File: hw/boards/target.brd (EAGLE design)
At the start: 25.4 x 25.4 mm, 21 parts, among them T1 771-BC847BS-T/R, U1 579-MCP1703T-3002ECB, U2 771-LPC824M201JDH20J, U4 579-MCP6291T-E/OT, X1 798-DF134P125V20

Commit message: Fix some part numbers
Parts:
- removed X1: 798-DF134P125V20, con-molex:53398-04
- added JP3: FTSH-105-01-L, torpedo:FTSH-105-01-XXX-DV-K
- JP2: value FTSH-105-01-L -> 798-DF134P125V20; device torpedo:FTSH-105-01-XXX-DV-K -> con-molex:53398-04
- moved JP2 12.6 mm to (21.6, 12.7)
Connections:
- net +3V3: now also JP3.1; no longer JP2.1
- net GND: now also JP2.4, JP3.3, JP3.5, JP3.9; no longer JP2.3, JP2.5, JP2.9, X1.4
- net RST: now also JP3.10; no longer JP2.10
- net RX: now also JP2.3; no longer X1.3
- net SWCLK: now also JP3.4; no longer JP2.4
- net SWDIO: now also JP3.2; no longer JP2.2
- net TX: now also JP2.2; no longer X1.2
- net VIN: now also JP2.1; no longer X1.1
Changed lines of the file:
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@@
 <attribute name="OC_FARNELL" value="1125367" x="3.81" y="12.7" size="1.778" layer="28" rot="MR270" display="off"/>
 </element>
-<element name="JP2" library="torpedo" package="FTSH-105-01-XXX-DV-K" value="FTSH-105-01-L" x="12.7" y="21.59" rot="MR90"/>
+<element name="JP3" library="torpedo" package="FTSH-105-01-XXX-DV-K" value="FTSH-105-01-L" x="12.7" y="21.59" rot="MR90"/>
 <element name="LOGO2" library="ohw-logo" package="OSHW_FILLX150_NOTEXT" value="OSHW_LOGO_FILLX0150-NT" x="6.604" y="5.588" rot="R90"/>
 <element name="R2" library="rcl" package="R0603" value="71-CRCW0603-5.6-E3" x="13.716" y="5.334" rot="MR90"/>
@@
 <attribute name="PROD_ID" value="IC-11991" x="18.288" y="5.334" size="1.778" layer="28" rot="MR270" display="off"/>
 </element>
-<element name="X1" library="con-molex" package="53398-04" value="798-DF134P125V20" x="21.59" y="12.7" rot="MR90">
+<element name="JP2" library="con-molex" package="53398-04" value="798-DF134P125V20" x="21.59" y="12.7" rot="MR90">
 <attribute name="OC_NEWARK" value="unknown" x="21.59" y="12.7" size="1.778" layer="28" rot="MR90" display="off"/>
 <attribute name="MPN" value="" x="21.59" y="12.7" size="1.778" layer="28" rot="MR90" display="off"/>
@@
 <contactref element="T1" pad="4"/>
 <contactref element="JP1" pad="4"/>
-<contactref element="X1" pad="4"/>
-<contactref element="JP2" pad="9"/>
-<contactref element="JP2" pad="5"/>
-<contactref element="JP2" pad="3"/>
+<contactref element="JP2" pad="4"/>
+<contactref element="JP3" pad="9"/>
+<contactref element="JP3" pad="5"/>
+<contactref element="JP3" pad="3"/>
 <contactref element="U1" pad="1"/>
 <contactref element="C2" pad="2"/>
@@
 <contactref element="D2" pad="2"/>
 <contactref element="U2" pad="15"/>
-<contactref element="JP2" pad="1"/>
+<contactref element="JP3" pad="1"/>
 <contactref element="R7" pad="1"/>
 <wire x1="6.416" y1="19.982" x2="6.516" y2="19.882" width="0.254" layer="16"/>
@@
 <contactref element="C1" pad="1"/>
 <contactref element="JP1" pad="1"/>
-<contactref element="X1" pad="1"/>
+<contactref element="JP2" pad="1"/>
 <wire x1="6.31" y1="10.825" x2="4.542" y2="10.825" width="0.6096" layer="16"/>
 <wire x1="4.542" y1="10.825" x2="4.064" y2="11.303" width="0.6096" layer="16"/>
@@
 <signal name="TX">
 <contactref element="JP1" pad="2"/>
-<contactref element="X1" pad="2"/>
+<contactref element="JP2" pad="2"/>
 <contactref element="U2" pad="3"/>
 <wire x1="11.075" y1="17.3958" x2="11.075" y2="15.595" width="0.254" layer="16"/>
@@
 <signal name="SWDIO">
 <contactref element="U2" pad="8"/>
-<contactref element="JP2" pad="2"/>
+<contactref element="JP3" pad="2"/>
 <wire x1="14.325" y1="17.3958" x2="14.325" y2="17.881" width="0.254" layer="16"/>
 <wire x1="14.325" y1="17.881" x2="14.732" y2="18.288" width="0.254" layer="16"/>
@@
 <signal name="SWCLK">
 <contactref element="U2" pad="7"/>
-<contactref element="JP2" pad="4"/>
+<contactref element="JP3" pad="4"/>
 <wire x1="14.732" y1="20.32" x2="13.208" y2="20.32" width="0.254" layer="16"/>
 <wire x1="13.208" y1="20.32" x2="12.954" y2="20.066" width="0.254" layer="16"/>
@@
 <signal name="RST">
 <contactref element="U2" pad="5"/>
-<contactref element="JP2" pad="10"/>
+<contactref element="JP3" pad="10"/>
 <contactref element="R7" pad="2"/>
 <wire x1="14.732" y1="24.13" x2="16.344" y2="24.13" width="0.254" layer="16"/>
@@
 <signal name="RX">
 <contactref element="JP1" pad="3"/>
-<contactref element="X1" pad="3"/>
+<contactref element="JP2" pad="3"/>
 <contactref element="U2" pad="2"/>
 <wire x1="6.31" y1="13.325" x2="8.499" y2="13.325" width="0.254" layer="16"/>

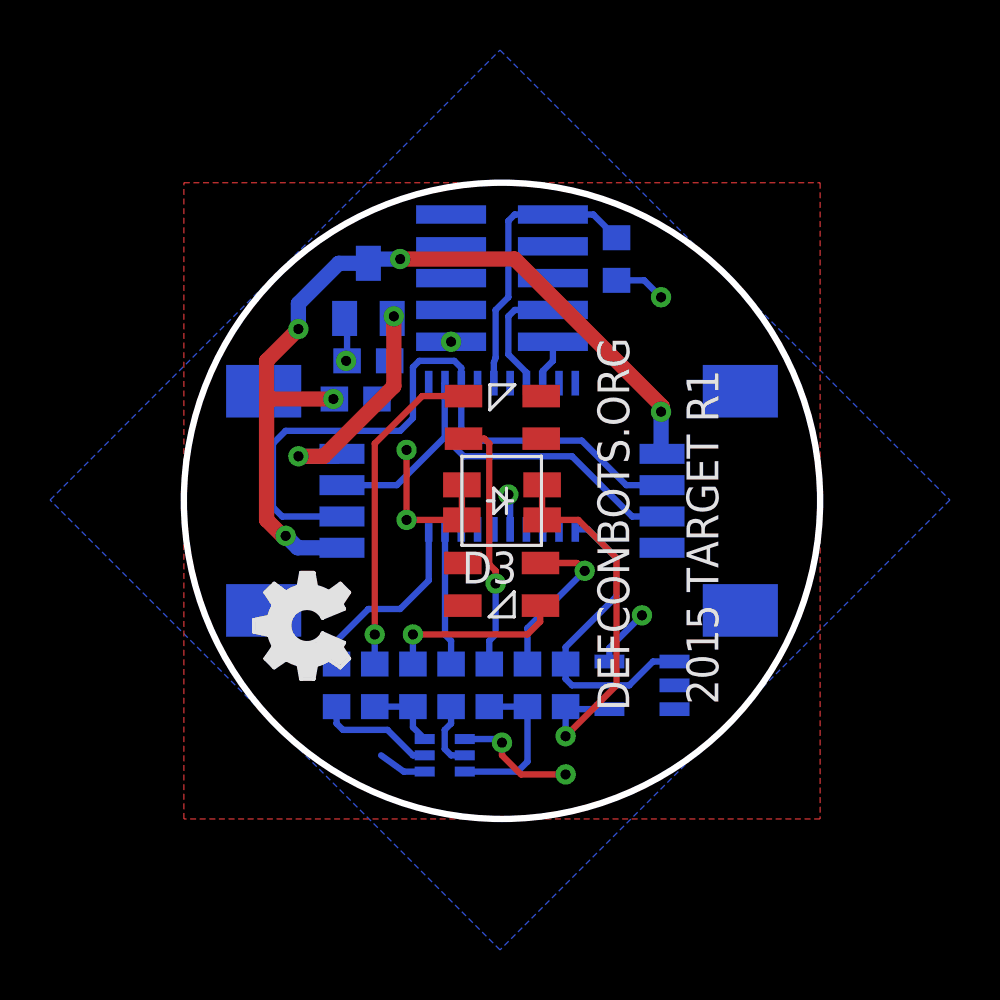
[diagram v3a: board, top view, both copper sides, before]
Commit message: Get rid of the panel, prep for proto order with dirty PCBs.
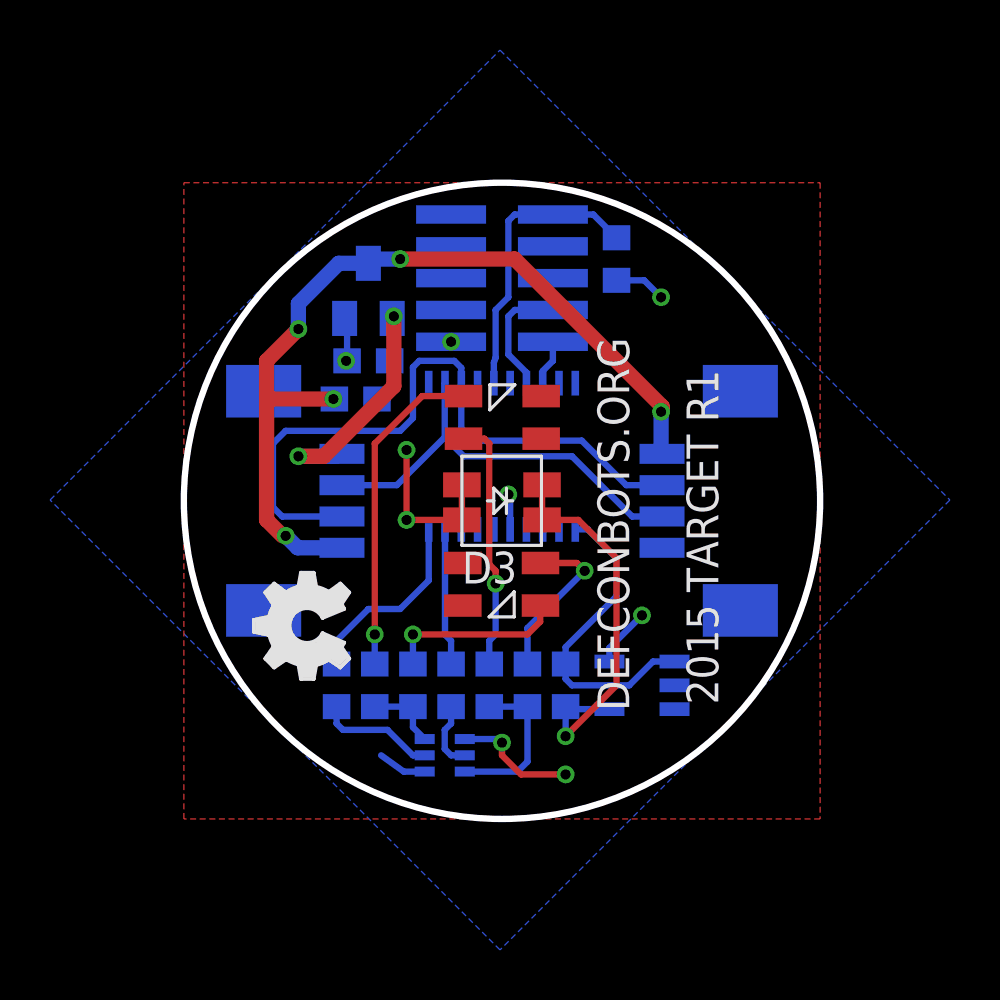
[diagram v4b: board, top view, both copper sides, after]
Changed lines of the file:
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@@
 </class>
 </classes>
-<designrules name="SSC-EAGLE-2Lyr_v1.0.0.3">
-<description language="en">&lt;b&gt;EAGLE Design Rules for *2* Layer Designs (DS)&lt;/b&gt;
-&lt;p&gt;
-This Sunstone Circuits 2 Layer .DRU has been set to cover our minimum requirements for our double sided products. For questions, comments, suggestions, please contact Sunstone Customer Support: &lt;p&gt;&lt;b&gt;Email:&lt;/b&gt;  mailto:support@sunstone.com&lt;br&gt;&lt;b&gt;Phone:&lt;/b&gt; 800-228-8198.&lt;p&gt; v1.1Mod10/16/07~Layers-core reversal.Distance C/D.Restring%.Supply G%.&lt;p&gt; v1.2 Mod12/06/07~Distance C/D to 20mils.&lt;p&gt;v1.3Mod12/12/07~Supply/Annulus Value to 12.5mils&lt;p&gt;1/15/08 SSC-EAGLE-2Lyr_v1.0.0.3~For Release&lt;p&gt;10/3/08 Description Edit.&lt;p&gt;
-&lt;p&gt;
-&lt;i&gt;Attention: Upon running the design check and making modifications, please remember to save any changes before closing the application and sending in your board file to Sunstone Circuits for conversion.&lt;i&gt;</description>
+<designrules name="dirt_cheap_dirty_boards.v1">
+<description language="en">&lt;b&gt;Dirty Cheap Dirty Board Design Rules&lt;/b&gt;
+&lt;br&gt;
+&lt;br&gt;Min width/Spacing: 5/5mil
+&lt;br&gt;Min diameter of finished hole 12mil</description>
 <param name="layerSetup" value="(1*16)"/>
-<param name="mtCopper" value="0.0178mm 0.0356mm 0.0356mm 0.0356mm 0.0356mm 0.0356mm 0.0356mm 0.0356mm 0.0356mm 0.0356mm 0.0356mm 0.0356mm 0.0356mm 0.0356mm 0.0356mm 0.0178mm"/>
-<param name="mtIsolate" value="59mil 0.1499mm 0.2007mm 0.1499mm 0.2007mm 0.1499mm 0.2007mm 0.1499mm 0.2007mm 0.1499mm 0.2007mm 0.1499mm 0.2007mm 0.1499mm 0.2007mm"/>
-<param name="mdWireWire" value="6mil"/>
-<param name="mdWirePad" value="6mil"/>
-<param name="mdWireVia" value="6mil"/>
-<param name="mdPadPad" value="6mil"/>
-<param name="mdPadVia" value="6mil"/>
-<param name="mdViaVia" value="6mil"/>
-<param name="mdSmdPad" value="6mil"/>
-<param name="mdSmdVia" value="6mil"/>
-<param name="mdSmdSmd" value="6mil"/>
+<param name="mtCopper" value="0.035mm 0.0175mm 0.035mm 0.035mm 0.035mm 0.035mm 0.035mm 0.035mm 0.035mm 0.035mm 0.035mm 0.035mm 0.035mm 0.035mm 0.0175mm 0.035mm"/>
+<param name="mtIsolate" value="1.5mm 1.1mm 0.2mm 0.15mm 0.2mm 0.15mm 0.2mm 0.15mm 0.2mm 0.15mm 0.2mm 0.15mm 0.2mm 0.15mm 0.2mm"/>
+<param name="mdWireWire" value="5mil"/>
+<param name="mdWirePad" value="5mil"/>
+<param name="mdWireVia" value="5mil"/>
+<param name="mdPadPad" value="5mil"/>
+<param name="mdPadVia" value="5mil"/>
+<param name="mdViaVia" value="5mil"/>
+<param name="mdSmdPad" value="0mil"/>
+<param name="mdSmdVia" value="0mil"/>
+<param name="mdSmdSmd" value="0mil"/>
 <param name="mdViaViaSameLayer" value="8mil"/>
 <param name="mnLayersViaInSmd" value="2"/>
-<param name="mdCopperDimension" value="20mil"/>
-<param name="mdDrill" value="16mil"/>
+<param name="mdCopperDimension" value="10mil"/>
+<param name="mdDrill" value="10mil"/>
 <param name="mdSmdStop" value="0mil"/>
-<param name="msWidth" value="6mil"/>
-<param name="msDrill" value="14mil"/>
-<param name="msMicroVia" value="9.9898mm"/>
+<param name="msWidth" value="5mil"/>
+<param name="msDrill" value="12mil"/>
+<param name="msMicroVia" value="12mil"/>
 <param name="msBlindViaRatio" value="0.5"/>
 <param name="rvPadTop" value="0.25"/>
@@
 <param name="rvMicroViaOuter" value="0.25"/>
 <param name="rvMicroViaInner" value="0.25"/>
-<param name="rlMinPadTop" value="8mil"/>
-<param name="rlMaxPadTop" value="999mil"/>
-<param name="rlMinPadInner" value="0mil"/>
-<param name="rlMaxPadInner" value="0mil"/>
-<param name="rlMinPadBottom" value="8mil"/>
-<param name="rlMaxPadBottom" value="999mil"/>
-<param name="rlMinViaOuter" value="8mil"/>
-<param name="rlMaxViaOuter" value="999mil"/>
-<param name="rlMinViaInner" value="0mil"/>
-<param name="rlMaxViaInner" value="0mil"/>
-<param name="rlMinMicroViaOuter" value="8mil"/>
-<param name="rlMaxMicroViaOuter" value="999mil"/>
-<param name="rlMinMicroViaInner" value="0mil"/>
-<param name="rlMaxMicroViaInner" value="0mil"/>
+<param name="rlMinPadTop" value="10mil"/>
+<param name="rlMaxPadTop" value="20mil"/>
+<param name="rlMinPadInner" value="10mil"/>
+<param name="rlMaxPadInner" value="20mil"/>
+<param name="rlMinPadBottom" value="10mil"/>
+<param name="rlMaxPadBottom" value="20mil"/>
+<param name="rlMinViaOuter" value="6mil"/>
+<param name="rlMaxViaOuter" value="20mil"/>
+<param name="rlMinViaInner" value="6mil"/>
+<param name="rlMaxViaInner" value="20mil"/>
+<param name="rlMinMicroViaOuter" value="4mil"/>
+<param name="rlMaxMicroViaOuter" value="20mil"/>
+<param name="rlMinMicroViaInner" value="4mil"/>
+<param name="rlMaxMicroViaInner" value="20mil"/>
 <param name="psTop" value="-1"/>
 <param name="psBottom" value="-1"/>
-<param name="psFirst" value="-1"/>
+<param name="psFirst" value="0"/>
 <param name="psElongationLong" value="100"/>
 <param name="psElongationOffset" value="100"/>
 <param name="mvStopFrame" value="1"/>
 <param name="mvCreamFrame" value="0"/>
-<param name="mlMinStopFrame" value="3mil"/>
-<param name="mlMaxStopFrame" value="3mil"/>
+<param name="mlMinStopFrame" value="2mil"/>
+<param name="mlMaxStopFrame" value="2mil"/>
 <param name="mlMinCreamFrame" value="0mil"/>
 <param name="mlMaxCreamFrame" value="0mil"/>
-<param name="mlViaStopLimit" value="0mil"/>
+<param name="mlViaStopLimit" value="25mil"/>
 <param name="srRoundness" value="0"/>
 <param name="srMinRoundness" value="0mil"/>
@@
 <param name="checkAngle" value="0"/>
 <param name="checkFont" value="1"/>
-<param name="checkRestrict" value="1"/>
+<param name="checkRestrict" value="0"/>
 <param name="useDiameter" value="13"/>
-<param name="maxErrors" value="500"/>
+<param name="maxErrors" value="50"/>
 </designrules>
 <autorouter>
